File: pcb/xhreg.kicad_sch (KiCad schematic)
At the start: 12 parts, among them Q1076 2N7002a, Q1077 2N7002a, Q1078 2N7002a, Q1079 2N7002a, Q1080 2N7002a, Q1081 2N7002a, Q1082 2N7002a, Q1083 2N7002a, Q1084 2N7002a, Q1085 2N7002a

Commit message: XH/XL.
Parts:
- renumbered Q1076 to Q750, Q1077 to Q751, Q1078 to Q752, Q1079 to Q753, Q1080 to Q754, Q1081 to Q755, Q1082 to Q756, Q1083 to Q757, Q1084 to Q758, Q1085 to Q759, R466 to R317, R467 to R318
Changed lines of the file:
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@@
     (effects (font (size 1.27 1.27)) (justify left))
   )
-  (symbol (lib_id "power:VCC") (at 67.31 104.14 0) (unit 1)
-    (in_bom yes) (on_board yes)
-    (property "Reference" "#PWR0981" (id 0) (at 67.31 107.95 0)
+  (symbol (lib_id "power:VCC") (at 67.31 104.14 0)
+    (in_bom yes) (on_board yes)
+    (property "Reference" "#PWR0659" (id 0) (at 67.31 107.95 0)
       (effects (font (size 1.27 1.27)) hide)
     )
@@
     (pin "1")
   )
-  (symbol (lib_id "power:VCC") (at 135.89 46.99 0) (unit 1)
-    (in_bom yes) (on_board yes)
-    (property "Reference" "#PWR0973" (id 0) (at 135.89 50.8 0)
+  (symbol (lib_id "power:VCC") (at 135.89 46.99 0)
+    (in_bom yes) (on_board yes)
+    (property "Reference" "#PWR0651" (id 0) (at 135.89 50.8 0)
       (effects (font (size 1.27 1.27)) hide)
     )
@@
     (pin "1")
   )
-  (symbol (lib_id "power:GND") (at 67.31 87.63 0) (unit 1)
-    (in_bom yes) (on_board yes)
-    (property "Reference" "#PWR0976" (id 0) (at 67.31 93.98 0)
+  (symbol (lib_id "power:GND") (at 67.31 87.63 0)
+    (in_bom yes) (on_board yes)
+    (property "Reference" "#PWR0654" (id 0) (at 67.31 93.98 0)
       (effects (font (size 1.27 1.27)) hide)
     )
@@
     (pin "1")
   )
-  (symbol (lib_id "power:GND") (at 67.31 130.81 0) (unit 1)
-    (in_bom yes) (on_board yes)
-    (property "Reference" "#PWR0982" (id 0) (at 67.31 137.16 0)
+  (symbol (lib_id "power:GND") (at 67.31 130.81 0)
+    (in_bom yes) (on_board yes)
+    (property "Reference" "#PWR0660" (id 0) (at 67.31 137.16 0)
       (effects (font (size 1.27 1.27)) hide)
     )
@@
     (pin "1")
   )
-  (symbol (lib_id "power:GND") (at 93.98 95.25 0) (unit 1)
-    (in_bom yes) (on_board yes)
-    (property "Reference" "#PWR0977" (id 0) (at 93.98 101.6 0)
+  (symbol (lib_id "power:GND") (at 93.98 95.25 0)
+    (in_bom yes) (on_board yes)
+    (property "Reference" "#PWR0655" (id 0) (at 93.98 101.6 0)
       (effects (font (size 1.27 1.27)) hide)
     )
@@
     (pin "1")
   )
-  (symbol (lib_id "power:GND") (at 119.38 96.52 0) (unit 1)
-    (in_bom yes) (on_board yes)
-    (property "Reference" "#PWR0979" (id 0) (at 119.38 102.87 0)
+  (symbol (lib_id "power:GND") (at 119.38 96.52 0)
+    (in_bom yes) (on_board yes)
+    (property "Reference" "#PWR0657" (id 0) (at 119.38 102.87 0)
       (effects (font (size 1.27 1.27)) hide)
     )
@@
     (pin "1")
   )
-  (symbol (lib_id "power:GND") (at 148.59 96.52 0) (unit 1)
-    (in_bom yes) (on_board yes)
-    (property "Reference" "#PWR0980" (id 0) (at 148.59 102.87 0)
+  (symbol (lib_id "power:GND") (at 148.59 96.52 0)
+    (in_bom yes) (on_board yes)
+    (property "Reference" "#PWR0658" (id 0) (at 148.59 102.87 0)
       (effects (font (size 1.27 1.27)) hide)
     )
@@
     (pin "1")
   )
-  (symbol (lib_id "power:GND") (at 205.74 63.5 90) (unit 1)
-    (in_bom yes) (on_board yes)
-    (property "Reference" "#PWR0974" (id 0) (at 212.09 63.5 0)
+  (symbol (lib_id "power:GND") (at 205.74 63.5 90)
+    (in_bom yes) (on_board yes)
+    (property "Reference" "#PWR0652" (id 0) (at 212.09 63.5 0)
       (effects (font (size 1.27 1.27)) hide)
     )
@@
     (pin "1")
   )
-  (symbol (lib_id "power:GND") (at 205.74 68.58 90) (unit 1)
-    (in_bom yes) (on_board yes)
-    (property "Reference" "#PWR0975" (id 0) (at 212.09 68.58 0)
+  (symbol (lib_id "power:GND") (at 205.74 68.58 90)
+    (in_bom yes) (on_board yes)
+    (property "Reference" "#PWR0653" (id 0) (at 212.09 68.58 0)
       (effects (font (size 1.27 1.27)) hide)
     )
@@
     (pin "1")
   )
-  (symbol (lib_id "power:GND") (at 240.03 95.25 0) (unit 1)
-    (in_bom yes) (on_board yes)
-    (property "Reference" "#PWR0978" (id 0) (at 240.03 101.6 0)
+  (symbol (lib_id "power:GND") (at 240.03 95.25 0)
+    (in_bom yes) (on_board yes)
+    (property "Reference" "#PWR0656" (id 0) (at 240.03 101.6 0)
       (effects (font (size 1.27 1.27)) hide)
     )
@@
     (pin "1")
   )
-  (symbol (lib_id "Device:R") (at 67.31 107.95 0) (unit 1)
-    (in_bom yes) (on_board yes)
-    (property "Reference" "R467" (id 0) (at 69.088 106.7816 0)
+  (symbol (lib_id "Device:R") (at 67.31 107.95 0)
+    (in_bom yes) (on_board yes)
+    (property "Reference" "R318" (id 0) (at 69.088 106.7816 0)
       (effects (font (size 1.27 1.27)) (justify left))
     )
@@
     (pin "2")
   )
-  (symbol (lib_id "Device:R") (at 135.89 50.8 0) (unit 1)
-    (in_bom yes) (on_board yes)
-    (property "Reference" "R466" (id 0) (at 137.668 49.6316 0)
+  (symbol (lib_id "Device:R") (at 135.89 50.8 0)
+    (in_bom yes) (on_board yes)
+    (property "Reference" "R317" (id 0) (at 137.668 49.6316 0)
       (effects (font (size 1.27 1.27)) (justify left))
     )
@@
     (pin "2")
   )
-  (symbol (lib_id "Transistor_FET:2N7002") (at 64.77 82.55 0) (unit 1)
-    (in_bom yes) (on_board yes)
-    (property "Reference" "Q1080" (id 0) (at 70.0024 81.3816 0)
+  (symbol (lib_id "Transistor_FET:2N7002") (at 64.77 82.55 0)
+    (in_bom yes) (on_board yes)
+    (property "Reference" "Q754" (id 0) (at 70.0024 81.3816 0)
       (effects (font (size 1.27 1.27)) (justify left))
     )
@@
     (pin "3")
   )
-  (symbol (lib_id "Transistor_FET:2N7002") (at 64.77 125.73 0) (unit 1)
-    (in_bom yes) (on_board yes)
-    (property "Reference" "Q1085" (id 0) (at 70.0024 124.5616 0)
+  (symbol (lib_id "Transistor_FET:2N7002") (at 64.77 125.73 0)
+    (in_bom yes) (on_board yes)
+    (property "Reference" "Q759" (id 0) (at 70.0024 124.5616 0)
       (effects (font (size 1.27 1.27)) (justify left))
     )
@@
     (pin "3")
   )
-  (symbol (lib_id "Transistor_FET:2N7002") (at 91.44 80.01 0) (unit 1)
-    (in_bom yes) (on_board yes)
-    (property "Reference" "Q1076" (id 0) (at 96.6724 78.8416 0)
+  (symbol (lib_id "Transistor_FET:2N7002") (at 91.44 80.01 0)
+    (in_bom yes) (on_board yes)
+    (property "Reference" "Q750" (id 0) (at 96.6724 78.8416 0)
       (effects (font (size 1.27 1.27)) (justify left))
     )
@@
     (pin "3")
   )
-  (symbol (lib_id "Transistor_FET:2N7002") (at 91.44 90.17 0) (unit 1)
-    (in_bom yes) (on_board yes)
-    (property "Reference" "Q1081" (id 0) (at 96.6724 89.0016 0)
+  (symbol (lib_id "Transistor_FET:2N7002") (at 91.44 90.17 0)
+    (in_bom yes) (on_board yes)
+    (property "Reference" "Q755" (id 0) (at 96.6724 89.0016 0)
       (effects (font (size 1.27 1.27)) (justify left))
     )
@@
     (pin "3")
   )
-  (symbol (lib_id "Transistor_FET:2N7002") (at 116.84 81.28 0) (unit 1)
-    (in_bom yes) (on_board yes)
-    (property "Reference" "Q1078" (id 0) (at 122.0724 80.1116 0)
+  (symbol (lib_id "Transistor_FET:2N7002") (at 116.84 81.28 0)
+    (in_bom yes) (on_board yes)
+    (property "Reference" "Q752" (id 0) (at 122.0724 80.1116 0)
       (effects (font (size 1.27 1.27)) (justify left))
     )
@@
     (pin "3")
   )
-  (symbol (lib_id "Transistor_FET:2N7002") (at 116.84 91.44 0) (unit 1)
-    (in_bom yes) (on_board yes)
-    (property "Reference" "Q1083" (id 0) (at 122.0724 90.2716 0)
+  (symbol (lib_id "Transistor_FET:2N7002") (at 116.84 91.44 0)
+    (in_bom yes) (on_board yes)
+    (property "Reference" "Q757" (id 0) (at 122.0724 90.2716 0)
       (effects (font (size 1.27 1.27)) (justify left))
     )
@@
     (pin "3")
   )
-  (symbol (lib_id "Transistor_FET:2N7002") (at 146.05 81.28 0) (unit 1)
-    (in_bom yes) (on_board yes)
-    (property "Reference" "Q1079" (id 0) (at 151.2824 80.1116 0)
+  (symbol (lib_id "Transistor_FET:2N7002") (at 146.05 81.28 0)
+    (in_bom yes) (on_board yes)
+    (property "Reference" "Q753" (id 0) (at 151.2824 80.1116 0)
       (effects (font (size 1.27 1.27)) (justify left))
     )
@@
     (pin "3")
   )
-  (symbol (lib_id "Transistor_FET:2N7002") (at 146.05 91.44 0) (unit 1)
-    (in_bom yes) (on_board yes)
-    (property "Reference" "Q1084" (id 0) (at 151.2824 90.2716 0)
+  (symbol (lib_id "Transistor_FET:2N7002") (at 146.05 91.44 0)
+    (in_bom yes) (on_board yes)
+    (property "Reference" "Q758" (id 0) (at 151.2824 90.2716 0)
       (effects (font (size 1.27 1.27)) (justify left))
     )
@@
     (pin "3")
   )
-  (symbol (lib_id "Transistor_FET:2N7002") (at 237.49 80.01 0) (unit 1)
-    (in_bom yes) (on_board yes)
-    (property "Reference" "Q1077" (id 0) (at 242.7224 78.8416 0)
+  (symbol (lib_id "Transistor_FET:2N7002") (at 237.49 80.01 0)
+    (in_bom yes) (on_board yes)
+    (property "Reference" "Q751" (id 0) (at 242.7224 78.8416 0)
       (effects (font (size 1.27 1.27)) (justify left))
     )
@@
     (pin "3")
   )
-  (symbol (lib_id "Transistor_FET:2N7002") (at 237.49 90.17 0) (unit 1)
-    (in_bom yes) (on_board yes)
-    (property "Reference" "Q1082" (id 0) (at 242.7224 89.0016 0)
-      (effects (font (size 1.27 1.27)) (justify left))
-    )
+  (symbol (lib_id "Transistor_FET:2N7002") (at 237.49 90.17 0)
+    (in_bom yes) (on_board yes)
+    (property "Reference" "Q756" (id 0) (at 242.7224 89.0016 0)
+      (effects (font (size 1.27 1.27)) (justify left))
+    )

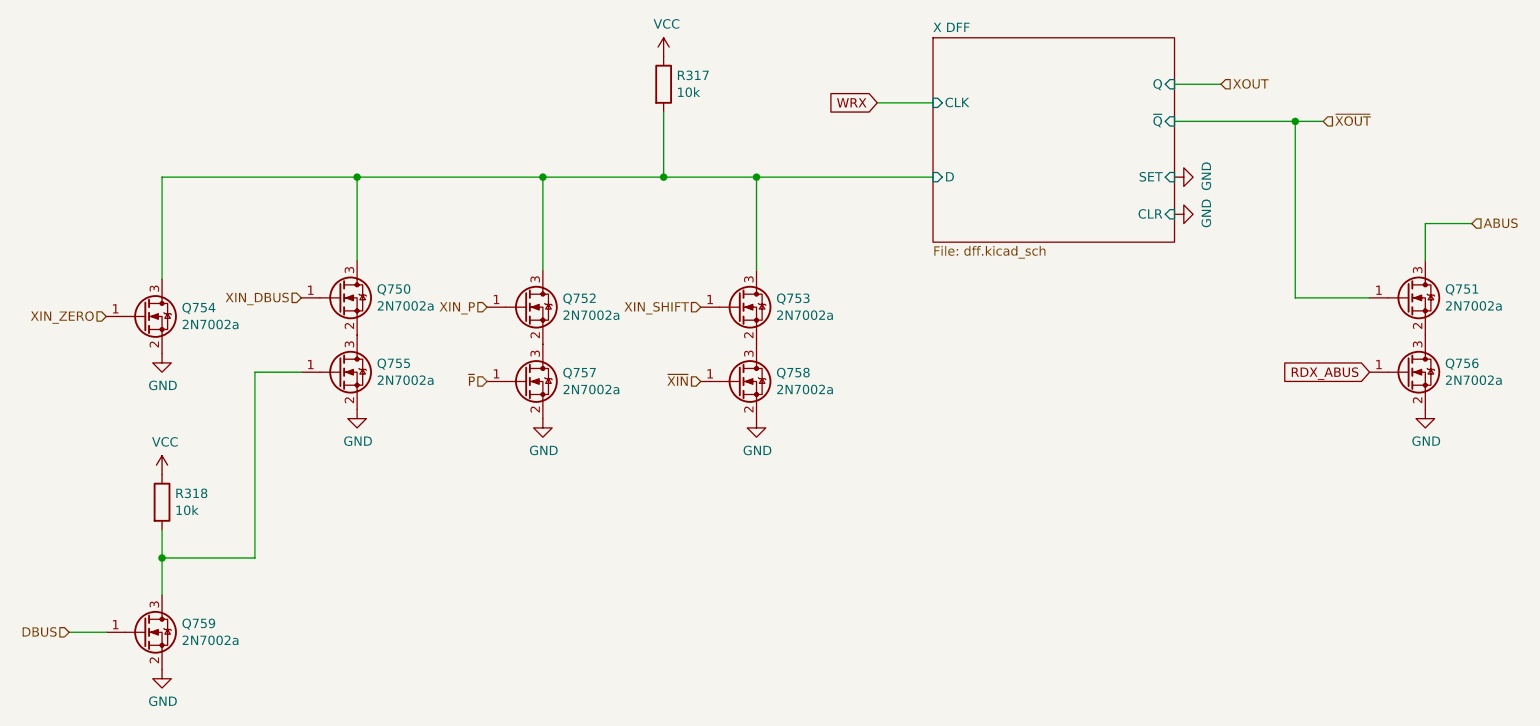
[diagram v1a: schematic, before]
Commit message: Fix UUIDs.
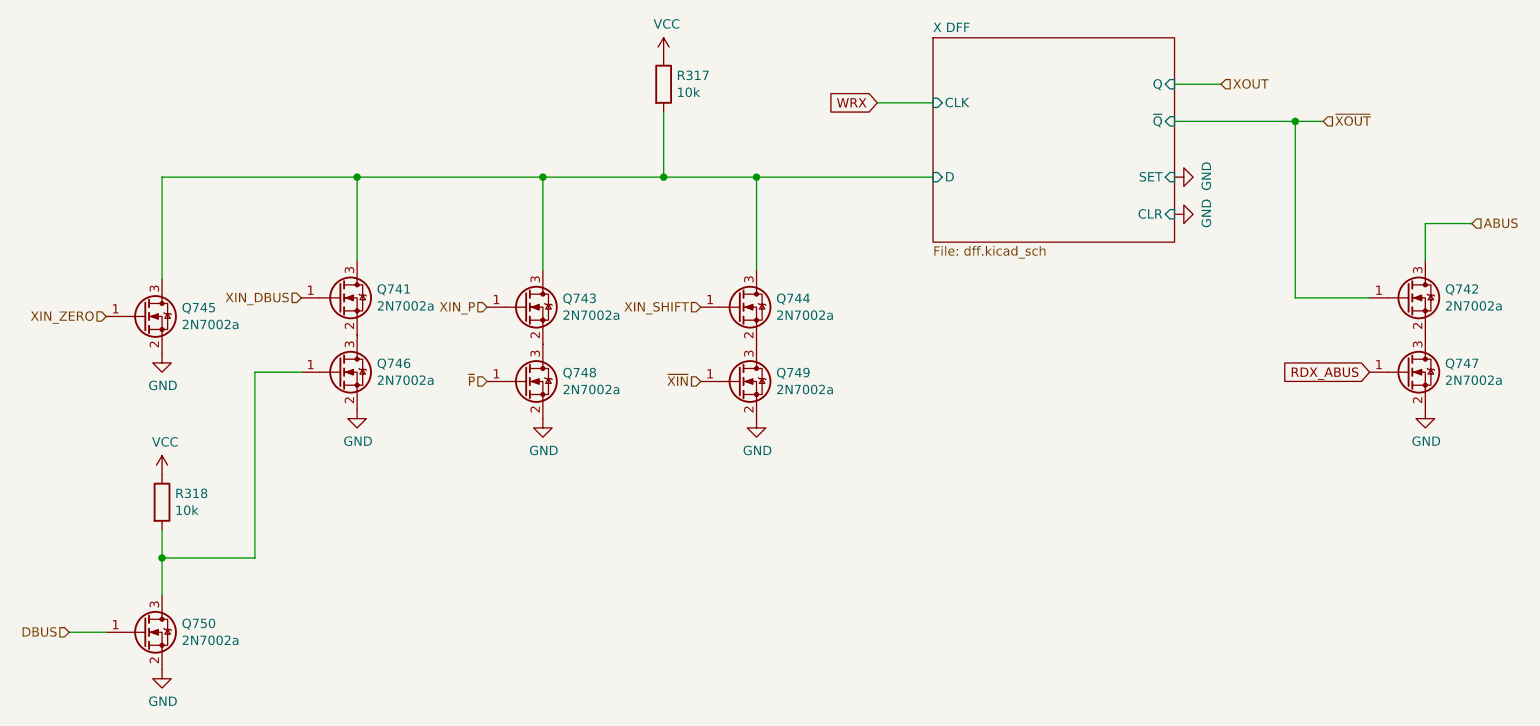
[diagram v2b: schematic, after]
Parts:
- removed Q751, Q752, Q753, Q754, Q755, Q756, Q757, Q758, Q759: 2N7002a, Package_TO_SOT_SMD:SOT-23, symbol Transistor_FET:2N7002
- added Q741, Q742, Q743, Q744, Q745, Q746, Q747, Q748, Q749: 2N7002a, Package_TO_SOT_SMD:SOT-23, symbol Transistor_FET:2N7002
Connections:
- net ABUS: now also Q742.3 (D)
- net DBUS: now also Q750.1 (G)
- net GND: now also Q750.2 (S), Q745.2 (S), Q746.2 (S), Q747.2 (S), Q748.2 (S), Q749.2 (S)
- net RDX_ABUS: now also Q747.1 (G)
- net X DFF/D: now also Q741.3 (D), Q743.3 (D), Q744.3 (D), Q745.3 (D); no longer Q750.3 (D)
- net XIN_DBUS: now also Q741.1 (G); no longer Q750.1 (G)
- net XIN_P: now also Q743.1 (G)
- net XIN_SHIFT: now also Q744.1 (G)
- net XIN_ZERO: now also Q745.1 (G)
- net ~P: now also Q748.1 (G)
- net ~XIN: now also Q749.1 (G)
- net ~XOUT: now also Q742.1 (G)
- net at R318.2: now also Q750.3 (D), Q746.1 (G)
- new net: Q744.2 (S), Q749.3 (D)
- new net: Q743.2 (S), Q748.3 (D)
- new net: Q742.2 (S), Q747.3 (D)
- new net: Q741.2 (S), Q746.3 (D)
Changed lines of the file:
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@@
   (symbol (lib_id "power:VCC") (at 67.31 104.14 0)
     (in_bom yes) (on_board yes)
-    (property "Reference" "#PWR0659" (id 0) (at 67.31 107.95 0)
+    (property "Reference" "#PWR0639" (id 0) (at 67.31 107.95 0)
       (effects (font (size 1.27 1.27)) hide)
     )
@@
   (symbol (lib_id "power:VCC") (at 135.89 46.99 0)
     (in_bom yes) (on_board yes)
-    (property "Reference" "#PWR0651" (id 0) (at 135.89 50.8 0)
+    (property "Reference" "#PWR0631" (id 0) (at 135.89 50.8 0)
       (effects (font (size 1.27 1.27)) hide)
     )
@@
   (symbol (lib_id "power:GND") (at 67.31 87.63 0)
     (in_bom yes) (on_board yes)
-    (property "Reference" "#PWR0654" (id 0) (at 67.31 93.98 0)
+    (property "Reference" "#PWR0634" (id 0) (at 67.31 93.98 0)
       (effects (font (size 1.27 1.27)) hide)
     )
@@
   (symbol (lib_id "power:GND") (at 67.31 130.81 0)
     (in_bom yes) (on_board yes)
-    (property "Reference" "#PWR0660" (id 0) (at 67.31 137.16 0)
+    (property "Reference" "#PWR0640" (id 0) (at 67.31 137.16 0)
       (effects (font (size 1.27 1.27)) hide)
     )
@@
   (symbol (lib_id "power:GND") (at 93.98 95.25 0)
     (in_bom yes) (on_board yes)
-    (property "Reference" "#PWR0655" (id 0) (at 93.98 101.6 0)
+    (property "Reference" "#PWR0635" (id 0) (at 93.98 101.6 0)
       (effects (font (size 1.27 1.27)) hide)
     )
@@
   (symbol (lib_id "power:GND") (at 119.38 96.52 0)
     (in_bom yes) (on_board yes)
-    (property "Reference" "#PWR0657" (id 0) (at 119.38 102.87 0)
+    (property "Reference" "#PWR0637" (id 0) (at 119.38 102.87 0)
       (effects (font (size 1.27 1.27)) hide)
     )
@@
   (symbol (lib_id "power:GND") (at 148.59 96.52 0)
     (in_bom yes) (on_board yes)
-    (property "Reference" "#PWR0658" (id 0) (at 148.59 102.87 0)
+    (property "Reference" "#PWR0638" (id 0) (at 148.59 102.87 0)
       (effects (font (size 1.27 1.27)) hide)
     )
@@
   (symbol (lib_id "power:GND") (at 205.74 63.5 90)
     (in_bom yes) (on_board yes)
-    (property "Reference" "#PWR0652" (id 0) (at 212.09 63.5 0)
+    (property "Reference" "#PWR0632" (id 0) (at 212.09 63.5 0)
       (effects (font (size 1.27 1.27)) hide)
     )
@@
   (symbol (lib_id "power:GND") (at 205.74 68.58 90)
     (in_bom yes) (on_board yes)
-    (property "Reference" "#PWR0653" (id 0) (at 212.09 68.58 0)
+    (property "Reference" "#PWR0633" (id 0) (at 212.09 68.58 0)
       (effects (font (size 1.27 1.27)) hide)
     )
@@
   (symbol (lib_id "power:GND") (at 240.03 95.25 0)
     (in_bom yes) (on_board yes)
-    (property "Reference" "#PWR0656" (id 0) (at 240.03 101.6 0)
+    (property "Reference" "#PWR0636" (id 0) (at 240.03 101.6 0)
       (effects (font (size 1.27 1.27)) hide)
     )
@@
   (symbol (lib_id "Transistor_FET:2N7002") (at 64.77 82.55 0)
     (in_bom yes) (on_board yes)
-    (property "Reference" "Q754" (id 0) (at 70.0024 81.3816 0)
+    (property "Reference" "Q745" (id 0) (at 70.0024 81.3816 0)
       (effects (font (size 1.27 1.27)) (justify left))
     )
@@
   (symbol (lib_id "Transistor_FET:2N7002") (at 64.77 125.73 0)
     (in_bom yes) (on_board yes)
-    (property "Reference" "Q759" (id 0) (at 70.0024 124.5616 0)
+    (property "Reference" "Q750" (id 0) (at 70.0024 124.5616 0)
       (effects (font (size 1.27 1.27)) (justify left))
     )
@@
   (symbol (lib_id "Transistor_FET:2N7002") (at 91.44 80.01 0)
     (in_bom yes) (on_board yes)
-    (property "Reference" "Q750" (id 0) (at 96.6724 78.8416 0)
+    (property "Reference" "Q741" (id 0) (at 96.6724 78.8416 0)
       (effects (font (size 1.27 1.27)) (justify left))
     )
@@
   (symbol (lib_id "Transistor_FET:2N7002") (at 91.44 90.17 0)
     (in_bom yes) (on_board yes)
-    (property "Reference" "Q755" (id 0) (at 96.6724 89.0016 0)
+    (property "Reference" "Q746" (id 0) (at 96.6724 89.0016 0)
       (effects (font (size 1.27 1.27)) (justify left))
     )
@@
   (symbol (lib_id "Transistor_FET:2N7002") (at 116.84 81.28 0)
     (in_bom yes) (on_board yes)
-    (property "Reference" "Q752" (id 0) (at 122.0724 80.1116 0)
+    (property "Reference" "Q743" (id 0) (at 122.0724 80.1116 0)
       (effects (font (size 1.27 1.27)) (justify left))
     )
@@
   (symbol (lib_id "Transistor_FET:2N7002") (at 116.84 91.44 0)
     (in_bom yes) (on_board yes)
-    (property "Reference" "Q757" (id 0) (at 122.0724 90.2716 0)
+    (property "Reference" "Q748" (id 0) (at 122.0724 90.2716 0)
       (effects (font (size 1.27 1.27)) (justify left))
     )
@@
   (symbol (lib_id "Transistor_FET:2N7002") (at 146.05 81.28 0)
     (in_bom yes) (on_board yes)
-    (property "Reference" "Q753" (id 0) (at 151.2824 80.1116 0)
+    (property "Reference" "Q744" (id 0) (at 151.2824 80.1116 0)
       (effects (font (size 1.27 1.27)) (justify left))
     )
@@
   (symbol (lib_id "Transistor_FET:2N7002") (at 146.05 91.44 0)
     (in_bom yes) (on_board yes)
-    (property "Reference" "Q758" (id 0) (at 151.2824 90.2716 0)
+    (property "Reference" "Q749" (id 0) (at 151.2824 90.2716 0)
       (effects (font (size 1.27 1.27)) (justify left))
     )
@@
   (symbol (lib_id "Transistor_FET:2N7002") (at 237.49 80.01 0)
     (in_bom yes) (on_board yes)
-    (property "Reference" "Q751" (id 0) (at 242.7224 78.8416 0)
+    (property "Reference" "Q742" (id 0) (at 242.7224 78.8416 0)
       (effects (font (size 1.27 1.27)) (justify left))
     )
@@
   (symbol (lib_id "Transistor_FET:2N7002") (at 237.49 90.17 0)
     (in_bom yes) (on_board yes)
-    (property "Reference" "Q756" (id 0) (at 242.7224 89.0016 0)
-      (effects (font (size 1.27 1.27)) (justify left))
-    )
+    (property "Reference" "Q747" (id 0) (at 242.7224 89.0016 0)
+      (effects (font (size 1.27 1.27)) (justify left))
+    )
